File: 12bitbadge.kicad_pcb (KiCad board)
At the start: 2 copper layers, 62.6 x 53.7 mm, 47 parts, among them J1 Conn_02x04_Counter_Clockwise, J2 Conn_02x04_Counter_Clockwise, J3 Conn_02x04_Counter_Clockwise, J4 Conn_02x03_Odd_Even, J5 Conn_02x03_Odd_Even, J6 Conn_02x03_Odd_Even, J7 Conn_02x03_Odd_Even, Q1 Q_PMOS_GSD, Q2 Q_PMOS_GSD, Q3 Q_PMOS_GSD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

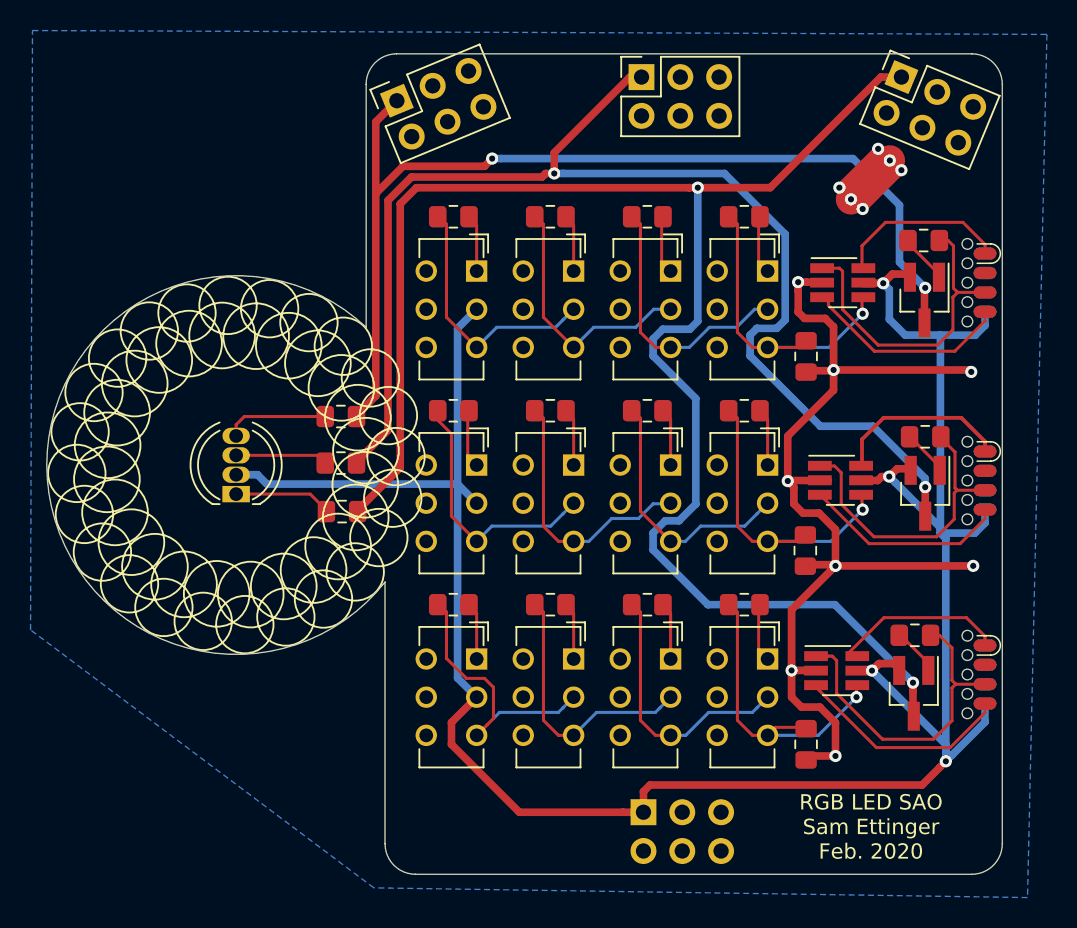
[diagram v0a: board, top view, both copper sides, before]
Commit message: Removed copper pour, so Oshpark After Dark would look cooler
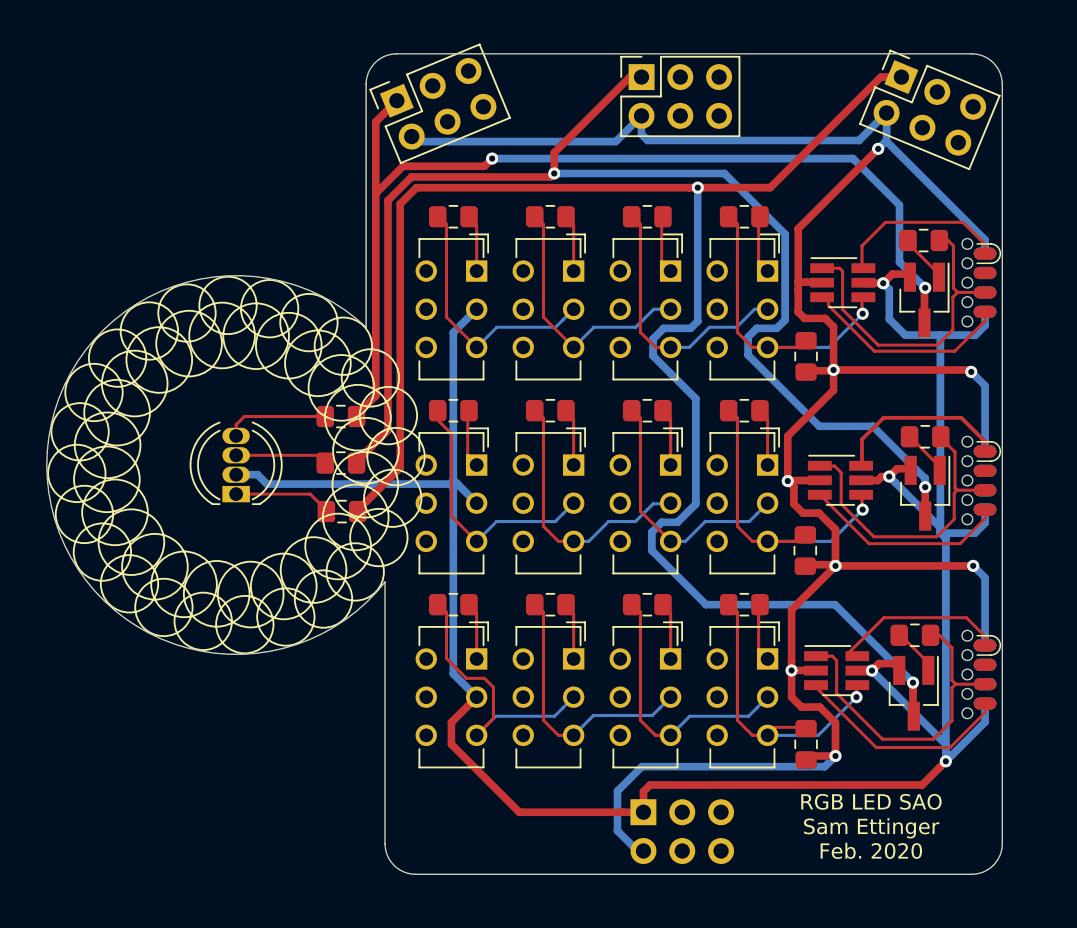
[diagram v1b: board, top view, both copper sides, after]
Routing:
- net 0V: track 78.3 -> 156.3 mm, vias 14 -> 8
- removed copper zone on B.Cu, net 0V

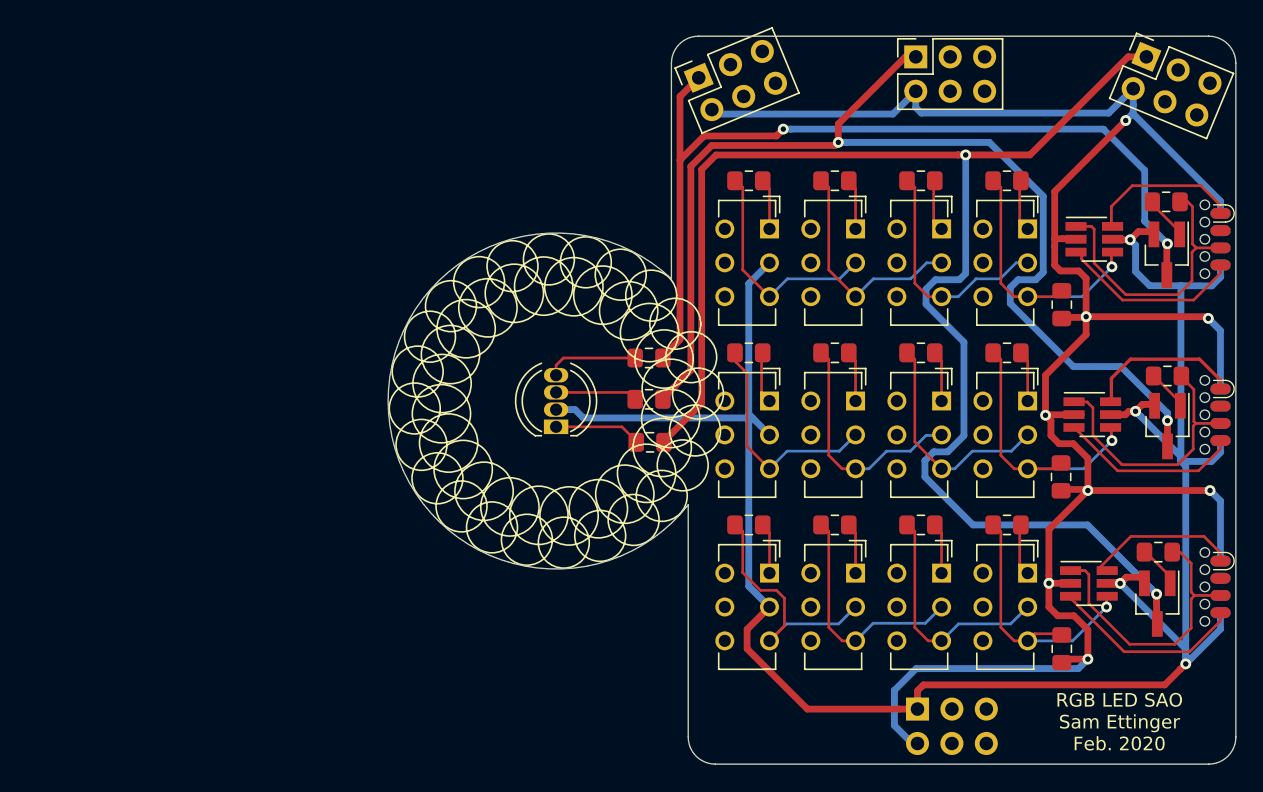
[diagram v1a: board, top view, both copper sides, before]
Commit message: Redesigning as a through-hole kit
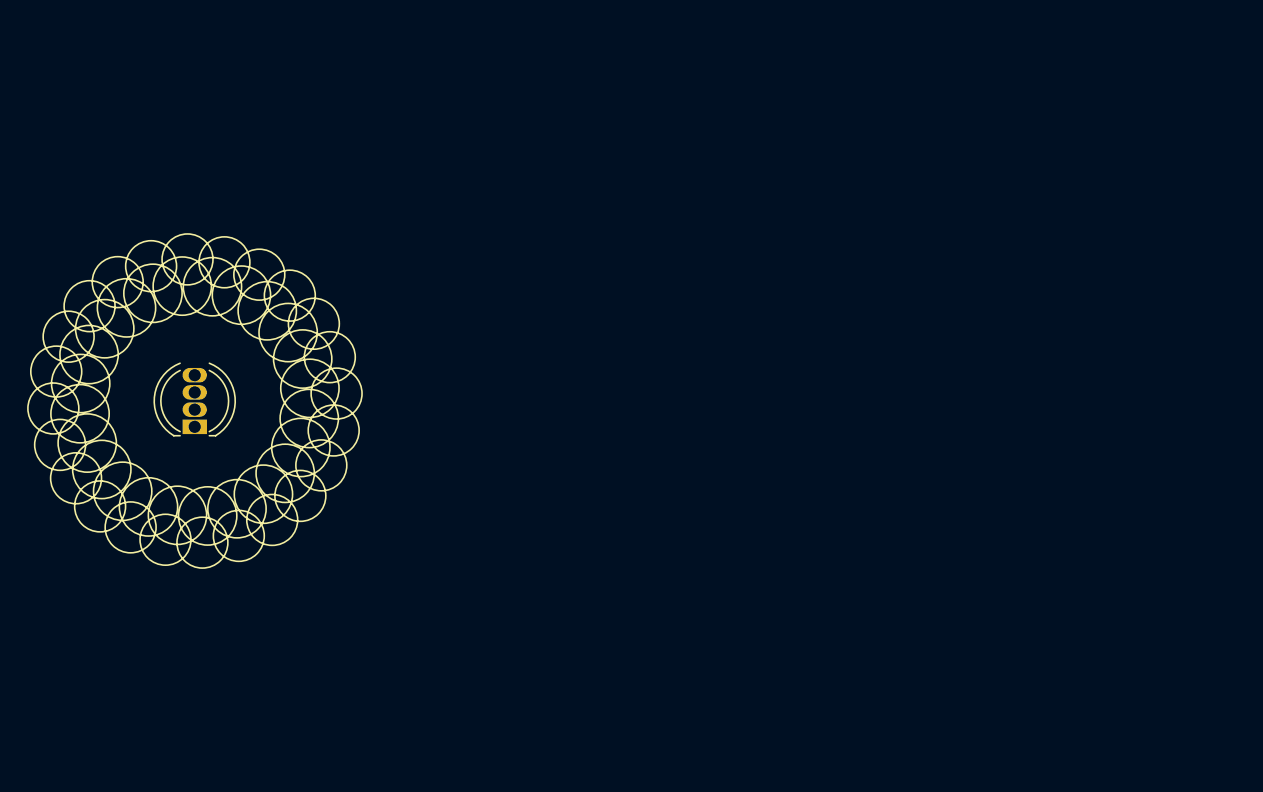
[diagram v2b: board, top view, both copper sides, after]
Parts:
- removed J1, J2, J3: Conn_02x04_Counter_Clockwise, 12bitbadge:SOIC_clipProgSmall
- removed J4: Conn_02x03_Odd_Even, Connector_PinHeader_2.54mm:PinHeader_2x03_P2.54mm_Vertical
- removed J5, J6, J7: Conn_02x03_Odd_Even, Connector_PinSocket_2.54mm:PinSocket_2x03_P2.54mm_Vertical
- removed Q1, Q2, Q3: Q_PMOS_GSD, Package_TO_SOT_SMD:SOT-23_Handsoldering
- removed R1, R10, R11, R15, R5, R6: 25k, Resistor_SMD:R_0805_2012Metric_Pad1.15x1.40mm_HandSolder
- removed R12, R2, R7: 50k, Resistor_SMD:R_0805_2012Metric_Pad1.15x1.40mm_HandSolder
- removed R13, R3, R8: 100k, Resistor_SMD:R_0805_2012Metric_Pad1.15x1.40mm_HandSolder
- removed R14, R4, R9: 200k, Resistor_SMD:R_0805_2012Metric_Pad1.15x1.40mm_HandSolder
- removed R16, R17, R18, R19, R20, R21: 1k, Resistor_SMD:R_0805_2012Metric_Pad1.15x1.40mm_HandSolder
- removed SW1, SW10, SW11, SW12, SW2, SW3, SW4, SW5, SW6, SW7, SW8, SW9: SW_SPDT, Button_Switch_THT:SW_CuK_JS202011CQN_DPDT_Straight
- removed U1, U2, U3: ATtiny10-TS, Package_TO_SOT_SMD:SOT-23-6_Handsoldering
- moved D1 26.7 mm to (115.1, 65.4)
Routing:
- net 0V: track 156.3 -> 0.00 mm, vias 8 -> 0
- net 3.3V: track 154.8 -> 0.00 mm, vias 4 -> 0
- net PWR_OUT_3: track 109.5 -> 0.00 mm, vias 2 -> 0
- net PWR_OUT_2: track 82.7 -> 0.00 mm, vias 2 -> 0
- net PWR_OUT_1: track 66.7 -> 0.00 mm, vias 2 -> 0
- net ADC_1: track 21.6 -> 0.00 mm, vias 1 -> 0
- net ADC_2: track 21.4 -> 0.00 mm, vias 1 -> 0
- net B_OUT: track 21.2 -> 0.00 mm
- net ADC_3: track 21.1 -> 0.00 mm, vias 1 -> 0
- net R_OUT: track 20.8 -> 0.00 mm
- net G_OUT: track 19.6 -> 0.00 mm
- net Net-(R11-Pad1): track 18.6 -> 0.00 mm
- net Net-(R7-Pad1): track 17.5 -> 0.00 mm
- net Net-(R12-Pad1): track 17.5 -> 0.00 mm
- net Net-(R13-Pad1): track 17.5 -> 0.00 mm
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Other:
- board outline removed
- board text removed: "RGB LED SAO Sam Ettinger Feb. 2020"

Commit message: Continued work on kit version
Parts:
- added C1: 10 nF, Capacitor_THT:C_Disc_D4.3mm_W1.9mm_P5.00mm, F.Cu at (133.3, 35.6)
- added C2: 10nF, Capacitor_THT:C_Disc_D4.3mm_W1.9mm_P5.00mm, F.Cu at (144.1, 30.1)
- added J1: Conn_02x03_Odd_Even, Connector_PinSocket_2.54mm:PinSocket_2x03_P2.54mm_Vertical, F.Cu at (190.9, -2.48)
- added J2: Conn_02x03_Odd_Even, Connector_PinSocket_2.54mm:PinSocket_2x03_P2.54mm_Vertical, F.Cu at (179.7, 10.0)
- added J3: Conn_02x03_Odd_Even, Connector_PinSocket_2.54mm:PinSocket_2x03_P2.54mm_Vertical, F.Cu at (168.9, 16.3)
- added J4: Conn_02x03_Odd_Even, Connector_PinHeader_2.54mm:PinHeader_2x03_P2.54mm_Vertical, F.Cu at (155.7, 22.5)
- added J5: Conn_02x03_Odd_Even, Connector_PinHeader_2.54mm:PinHeader_2x03_P2.54mm_Vertical, F.Cu at (125.2, 12.7)
- added Q1: Q_PMOS_GDS, Package_TO_SOT_SMD:TO-252-2, F.Cu at (174.0, 61.7)
- added Q2: Q_PMOS_GDS, Package_TO_SOT_SMD:TO-252-2, F.Cu at (174.0, 77.2)
- added Q3: Q_PMOS_GDS, Package_TO_SOT_SMD:TO-252-2, F.Cu at (173.7, 92.5)
- added Q4: Q_PMOS_GDS, Package_TO_SOT_SMD:TO-252-2, F.Cu at (229.3, 29.6)
- added R1: 25k, Resistor_THT:R_Axial_DIN0204_L3.6mm_D1.6mm_P5.08mm_Horizontal, F.Cu at (139.2, 55.6)
- added R10: 25k, Resistor_THT:R_Axial_DIN0204_L3.6mm_D1.6mm_P5.08mm_Horizontal, F.Cu at (139.2, 70.9)
- added R11: 50k, Resistor_THT:R_Axial_DIN0204_L3.6mm_D1.6mm_P5.08mm_Horizontal, F.Cu at (146.8, 70.9)
- added R12: 100k, Resistor_THT:R_Axial_DIN0204_L3.6mm_D1.6mm_P5.08mm_Horizontal, F.Cu at (159.5, 70.9)
- added R13: 200k, Resistor_THT:R_Axial_DIN0204_L3.6mm_D1.6mm_P5.08mm_Horizontal, F.Cu at (162.1, 70.9)
- added R14: 25k, Resistor_THT:R_Axial_DIN0204_L3.6mm_D1.6mm_P5.08mm_Horizontal, F.Cu at (144.3, 83.6)
- added R15: 50k, Resistor_THT:R_Axial_DIN0204_L3.6mm_D1.6mm_P5.08mm_Horizontal, F.Cu at (151.9, 83.6)
- added R16: 100k, Resistor_THT:R_Axial_DIN0204_L3.6mm_D1.6mm_P5.08mm_Horizontal, F.Cu at (159.5, 83.6)
- added R17: 200k, Resistor_THT:R_Axial_DIN0204_L3.6mm_D1.6mm_P5.08mm_Horizontal, F.Cu at (167.1, 83.6)
- added R18: 1k, Resistor_THT:R_Axial_DIN0204_L3.6mm_D1.6mm_P5.08mm_Horizontal, F.Cu at (167.1, 74.7)
- added R19: 25k, Resistor_THT:R_Axial_DIN0204_L3.6mm_D1.6mm_P5.08mm_Horizontal, F.Cu at (139.2, 86.1)
- added R2: 50k, Resistor_THT:R_Axial_DIN0204_L3.6mm_D1.6mm_P5.08mm_Horizontal, F.Cu at (146.8, 55.6)
- added R20: 50k, Resistor_THT:R_Axial_DIN0204_L3.6mm_D1.6mm_P5.08mm_Horizontal, F.Cu at (146.8, 86.1)
- added R21: 100k, Resistor_THT:R_Axial_DIN0204_L3.6mm_D1.6mm_P5.08mm_Horizontal, F.Cu at (154.4, 86.1)
- added R22: 200k, Resistor_THT:R_Axial_DIN0204_L3.6mm_D1.6mm_P5.08mm_Horizontal, F.Cu at (162.1, 86.1)
- added R23: 25k, Resistor_THT:R_Axial_DIN0204_L3.6mm_D1.6mm_P5.08mm_Horizontal, F.Cu at (144.3, 98.8)
- added R24: 50k, Resistor_THT:R_Axial_DIN0204_L3.6mm_D1.6mm_P5.08mm_Horizontal, F.Cu at (151.9, 98.8)
- added R25: 100k, Resistor_THT:R_Axial_DIN0204_L3.6mm_D1.6mm_P5.08mm_Horizontal, F.Cu at (159.5, 98.8)
- added R26: 200k, Resistor_THT:R_Axial_DIN0204_L3.6mm_D1.6mm_P5.08mm_Horizontal, F.Cu at (167.1, 98.8)
- added R27: 1k, Resistor_THT:R_Axial_DIN0204_L3.6mm_D1.6mm_P5.08mm_Horizontal, F.Cu at (167.1, 89.9)
- added R28: 1k, Resistor_THT:R_Axial_DIN0204_L3.6mm_D1.6mm_P5.08mm_Horizontal, F.Cu at (199.5, 9.37)
- added R29: 1k, Resistor_THT:R_Axial_DIN0204_L3.6mm_D1.6mm_P5.08mm_Horizontal, F.Cu at (168.1, 31.5)
- added R3: 100k, Resistor_THT:R_Axial_DIN0204_L3.6mm_D1.6mm_P5.08mm_Horizontal, F.Cu at (154.4, 55.6)
- added R30: 1k, Resistor_THT:R_Axial_DIN0204_L3.6mm_D1.6mm_P5.08mm_Horizontal, F.Cu at (188.8, 19.1)
- added R31: 100k, Resistor_THT:R_Axial_DIN0204_L3.6mm_D1.6mm_P5.08mm_Horizontal, F.Cu at (176.1, 34.7)
- added R32: 1k, Resistor_THT:R_Axial_DIN0204_L3.6mm_D1.6mm_P5.08mm_Horizontal, F.Cu at (196.8, 15.9)
- added R33: 100k, Resistor_THT:R_Axial_DIN0204_L3.6mm_D1.6mm_P5.08mm_Horizontal, F.Cu at (186.1, 22.2)
- added R4: 200k, Resistor_THT:R_Axial_DIN0204_L3.6mm_D1.6mm_P5.08mm_Horizontal, F.Cu at (162.1, 55.6)
- added R5: 25k, Resistor_THT:R_Axial_DIN0204_L3.6mm_D1.6mm_P5.08mm_Horizontal, F.Cu at (139.2, 68.3)
- added R6: 50k, Resistor_THT:R_Axial_DIN0204_L3.6mm_D1.6mm_P5.08mm_Horizontal, F.Cu at (151.9, 68.3)
- added R7: 100k, Resistor_THT:R_Axial_DIN0204_L3.6mm_D1.6mm_P5.08mm_Horizontal, F.Cu at (159.5, 68.3)
- added R8: 200k, Resistor_THT:R_Axial_DIN0204_L3.6mm_D1.6mm_P5.08mm_Horizontal, F.Cu at (167.1, 68.3)
- added R9: 1k, Resistor_THT:R_Axial_DIN0204_L3.6mm_D1.6mm_P5.08mm_Horizontal, F.Cu at (167.1, 59.4)
- added RV1: 100kΩ, Potentiometer_THT:Potentiometer_Alpha_RD901F-40-00D_Single_Vertical_CircularHoles, F.Cu at (112.4, 94.6)
- added SW1: SW_SPDT, Button_Switch_THT:SW_CuK_JS202011CQN_DPDT_Straight, F.Cu at (146.1, 59.4)
- added SW10: SW_SPDT, Button_Switch_THT:SW_CuK_JS202011CQN_DPDT_Straight, F.Cu at (151.9, 89.9)
- added SW11: SW_SPDT, Button_Switch_THT:SW_CuK_JS202011CQN_DPDT_Straight, F.Cu at (157.7, 89.9)
- added SW12: SW_SPDT, Button_Switch_THT:SW_CuK_JS202011CQN_DPDT_Straight, F.Cu at (163.6, 89.9)
- added SW2: SW_SPDT, Button_Switch_THT:SW_CuK_JS202011CQN_DPDT_Straight, F.Cu at (151.9, 59.4)
- added SW3: SW_SPDT, Button_Switch_THT:SW_CuK_JS202011CQN_DPDT_Straight, F.Cu at (157.7, 59.4)
- added SW4: SW_SPDT, Button_Switch_THT:SW_CuK_JS202011CQN_DPDT_Straight, F.Cu at (163.8, 59.4)
- added SW5: SW_SPDT, Button_Switch_THT:SW_CuK_JS202011CQN_DPDT_Straight, F.Cu at (146.0, 74.7)
- added SW6: SW_SPDT, Button_Switch_THT:SW_CuK_JS202011CQN_DPDT_Straight, F.Cu at (151.9, 74.7)
- added SW7: SW_SPDT, Button_Switch_THT:SW_CuK_JS202011CQN_DPDT_Straight, F.Cu at (157.7, 74.7)
- added SW8: SW_SPDT, Button_Switch_THT:SW_CuK_JS202011CQN_DPDT_Straight, F.Cu at (163.6, 74.7)
- added SW9: SW_SPDT, Button_Switch_THT:SW_CuK_JS202011CQN_DPDT_Straight, F.Cu at (146.1, 89.9)
- added U1: TLC555CP, Package_DIP:DIP-8_W7.62mm, F.Cu at (148.2, -2.73)
- added U2: ATtiny85-20PU, Package_DIP:DIP-8_W7.62mm, F.Cu at (133.4, 11.7)

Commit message: Kit version looks okay
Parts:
- J4: moved to B.Cu
- moved Q4 118.9 mm to (118.6, 72.9), turned to 180 degrees
- moved R32 103.7 mm to (116.3, 81.3)
- moved J1 93.1 mm to (114.6, 50.8), turned to 112.5 degrees
- moved R33 89.3 mm to (121.4, 83.8), turned to 180 degrees
- moved U1 80.1 mm to (127.8, 74.7)
- moved D1 78.5 mm to (192.5, 77.9)
- moved J4 77.7 mm to (130.6, 96.0), turned to 270 degrees
- moved R30 76.8 mm to (179.1, 95.2), turned to 90 degrees
- moved R31 70.2 mm to (121.4, 78.7), turned to 180 degrees
- moved C2 62.1 mm to (129.6, 90.4)
- moved R28 54.3 mm to (179.1, 59.7), turned to 270 degrees
- moved C1 52.1 mm to (134.6, 87.6), turned to 180 degrees
- moved J2 51.9 mm to (143.8, 47.5), turned to 90 degrees
- moved U2 49.4 mm to (127.8, 60.7)
- moved J5 48.1 mm to (117.3, 60.2)
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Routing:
- net 0V: track 0.00 -> 186.4 mm
- net 3.3V: track 0.00 -> 173.2 mm, vias 0 -> 2
- net ADC_1: track 0.00 -> 81.1 mm
- net PWR_OUT_1: track 0.00 -> 72.8 mm, vias 0 -> 1
- net ADC_3: track 0.00 -> 66.0 mm
- net ADC_2: track 0.00 -> 65.9 mm
- net B_OUT: track 0.00 -> 65.0 mm
- net R_OUT: track 0.00 -> 63.4 mm
- net PWR_OUT_2: track 0.00 -> 63.2 mm, vias 0 -> 1
- net G_OUT: track 0.00 -> 62.4 mm
- net PWR_OUT_3: track 0.00 -> 55.2 mm, vias 0 -> 1
- net PWR_IN: track 0.00 -> 54.4 mm
- net Net-(C1-Pad1): track 0.00 -> 31.7 mm
- net Net-(R1-Pad1): track 0.00 -> 24.5 mm
- net Net-(R3-Pad1): track 0.00 -> 24.2 mm
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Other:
- board outline added: 94.2 x 54.1 mm
